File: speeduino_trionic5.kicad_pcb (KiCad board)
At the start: 2 copper layers, 152.4 x 127 mm, 30 parts, among them J3 trionic5_header, Q1 Q_NMOS_GDS, U1 Olimex_STM32-407_Extension_He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, U2 MCP2515_Breakout, U3 LM1815, U8 LM2940S-5.0/NOPB

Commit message: Boards should be placed correctly now
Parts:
- removed F1: Polyfuse, Fuse:Fuse_1812_4532Metric
- added D1: LED, LED_SMD:LED_0603_1608Metric, F.Cu at (-47.4, 109.2)
- added D10: LED, LED_SMD:LED_0603_1608Metric, F.Cu at (-35.2, 98.3)
- added D11: LED, LED_SMD:LED_0603_1608Metric, F.Cu at (-71.7, 125.3)
- added D12: LED, LED_SMD:LED_0603_1608Metric, F.Cu at (-79.8, 125.3)
- added D13: LED, LED_SMD:LED_0603_1608Metric, F.Cu at (-83.8, 125.3)
- added D16: LED, LED_SMD:LED_0603_1608Metric, F.Cu at (-35.2, 95.7)
- added D17: LED, LED_SMD:LED_0603_1608Metric, F.Cu at (-24.5, 114.3)
- added D18: LED, LED_SMD:LED_0603_1608Metric, F.Cu at (-20.4, 114.3)
- added D3: LED, LED_SMD:LED_0603_1608Metric, F.Cu at (-59.5, 119.9)
- added D4: LED, LED_SMD:LED_0603_1608Metric, F.Cu at (-55.5, 117.3)
- added D5: LED, LED_SMD:LED_0603_1608Metric, F.Cu at (-75.7, 125.3)
- added D6: LED, LED_SMD:LED_0603_1608Metric, F.Cu at (-63.6, 125.3)
- added D7: LED, LED_SMD:LED_0603_1608Metric, F.Cu at (-59.5, 117.3)
- added D8: LED, LED_SMD:LED_0603_1608Metric, F.Cu at (-67.6, 125.3)
- added D9: LED, LED_SMD:LED_0603_1608Metric, F.Cu at (-35.2, 93.1)
- added Q1: Q_NMOS_GDS, Package_TO_SOT_SMD:TO-252-2, F.Cu at (-55.5, 103.9)
- added Q10: Q_NMOS_GDS, Package_TO_SOT_SMD:TO-252-2, F.Cu at (-67.7, 112.0)
- added Q11: Q_NMOS_GDS, Package_TO_SOT_SMD:TO-252-2, F.Cu at (-79.8, 103.9)
- added Q12: Q_NMOS_GDS, Package_TO_SOT_SMD:TO-252-2, F.Cu at (-43.4, 103.9)
- added Q13: Q_NMOS_GDS, Package_TO_SOT_SMD:TO-252-2, F.Cu at (-67.7, 103.9)
- added Q14: Q_NMOS_GDS, Package_TO_SOT_SMD:TO-252-2, F.Cu at (-20.4, 109.0)
- added Q15: Q_NMOS_GDS, Package_TO_SOT_SMD:TO-252-2, F.Cu at (-8.04, 103.1)
- added Q2: Q_NMOS_GDS, Package_TO_SOT_SMD:TO-252-2, F.Cu at (-79.8, 120.0)
- added Q3: Q_NMOS_GDS, Package_TO_SOT_SMD:TO-252-2, F.Cu at (-67.7, 120.0)
- added Q4: Q_NMOS_GDS, Package_TO_SOT_SMD:TO-252-2, F.Cu at (-79.8, 95.8)
- added Q5: Q_NMOS_GDS, Package_TO_SOT_SMD:TO-252-2, F.Cu at (-55.5, 112.0)
- added Q6: Q_NMOS_GDS, Package_TO_SOT_SMD:TO-252-2, F.Cu at (-43.4, 95.8)
- added Q7: Q_NMOS_GDS, Package_TO_SOT_SMD:TO-252-2, F.Cu at (-67.7, 95.8)
- added Q8: Q_NMOS_GDS, Package_TO_SOT_SMD:TO-252-2, F.Cu at (-55.5, 95.8)
- added Q9: Q_NMOS_GDS, Package_TO_SOT_SMD:TO-252-2, F.Cu at (-79.8, 112.0)
- added R10: 1k, Resistor_SMD:R_0603_1608Metric, F.Cu at (-27.2, 98.1)
- added R11: 1k, Resistor_SMD:R_0603_1608Metric, F.Cu at (-31.2, 93.1)
- added R12: 1k, Resistor_SMD:R_0603_1608Metric, F.Cu at (-47.4, 116.8)
- added R13: 1k, Resistor_SMD:R_0603_1608Metric, F.Cu at (-31.2, 95.6)
- added R14: 1k, Resistor_SMD:R_0603_1608Metric, F.Cu at (-27.2, 93.1)
- added R15: 1k, Resistor_SMD:R_0603_1608Metric, F.Cu at (-47.4, 114.3)
- added R16: 1k, Resistor_SMD:R_0603_1608Metric, F.Cu at (-43.4, 109.2)
- added R17: 1k, Resistor_SMD:R_0603_1608Metric, F.Cu at (-35.3, 103.4)
- added R18: 1k, Resistor_SMD:R_0603_1608Metric, F.Cu at (-35.3, 100.8)
- added R19: 1k, Resistor_SMD:R_0603_1608Metric, F.Cu at (-55.5, 122.3)
- added R20: 1k, Resistor_SMD:R_0603_1608Metric, F.Cu at (-39.4, 109.2)
- added R21: 1k, Resistor_SMD:R_0603_1608Metric, F.Cu at (-59.6, 122.4)
- added R22: 1k, Resistor_SMD:R_0603_1608Metric, F.Cu at (-23.2, 93.1)
- added R23: 1k, Resistor_SMD:R_0603_1608Metric, F.Cu at (-51.5, 122.2)
- added R24: 1k, Resistor_SMD:R_0603_1608Metric, F.Cu at (-27.2, 95.6)
- added R25: 1k, Resistor_SMD:R_0603_1608Metric, F.Cu at (-59.6, 124.9)
- added R26: 1k, Resistor_SMD:R_0603_1608Metric, F.Cu at (-55.6, 124.8)
- added R27: 1k, Resistor_SMD:R_0603_1608Metric, F.Cu at (-51.5, 119.7)
- added R28: 1k, Resistor_SMD:R_0603_1608Metric, F.Cu at (-43.4, 114.3)
- added R29: 1k, Resistor_SMD:R_0603_1608Metric, F.Cu at (-47.4, 111.8)
- added R30: 1k, Resistor_SMD:R_0603_1608Metric, F.Cu at (-31.2, 98.1)
- added R31: 1k, Resistor_SMD:R_0603_1608Metric, F.Cu at (-55.5, 119.8)
- added R32: 1k, Resistor_SMD:R_0603_1608Metric, F.Cu at (-35.3, 105.9)
- added R33: 1k, Resistor_SMD:R_0603_1608Metric, F.Cu at (-16.5, 116.8)
- added R34: 1k, Resistor_SMD:R_0603_1608Metric, F.Cu at (-12.5, 114.3)
- added R35: 1k, Resistor_SMD:R_0603_1608Metric, F.Cu at (-20.5, 116.8)
- added R36: 1k, Resistor_SMD:R_0603_1608Metric, F.Cu at (-24.5, 116.8)
- added R7: 1k, Resistor_SMD:R_0603_1608Metric, F.Cu at (-31.3, 100.8)
- added R8: 1k, Resistor_SMD:R_0603_1608Metric, F.Cu at (-51.5, 117.2)
- added R9: 1k, Resistor_SMD:R_0603_1608Metric, F.Cu at (-43.4, 111.8)
- J3: moved to B.Cu
- U1, XA1, XA2: moved to F.Cu
- U8: footprint Package_TO_SOT_SMD:TO-263-3_TabPin2 -> Package_TO_SOT_SMD:SOT-223
- moved J3 90.7 mm to (71.8, 35.0), turned to 0 degrees
- moved U1 85.7 mm to (106.7, 68.6), turned to 0 degrees
- moved XA2 56.4 mm to (175.3, 132.1)
- moved XA1 49.9 mm to (96.5, 149.9)
- moved D2 48.7 mm to (-55.0, 149.9)
- moved U8 26.7 mm to (-45.7, 25.4)
- moved C17 16.2 mm to (-41.1, 44.7)
- moved D15 16.2 mm to (-24.2, 32.2)
- moved C21 16.2 mm to (-17.0, 31.6)
- moved C18 16.2 mm to (-25.9, 41.4)
- moved C20 16.2 mm to (-19.2, 36.4)
- moved D14 16.2 mm to (-32.2, 44.0)
- moved Q1 15.5 mm to (-29.6, 152.4)
- moved R3 15.5 mm to (-33.2, 143.0)
- moved R4 15.5 mm to (-32.0, 126.4)
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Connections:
- net VDD renamed Net-(C20-Pad1)
- J3 pad 10: unconnected-(J3-Pad10) -> T5_IGN2
- J3 pad 11: unconnected-(J3-Pad11) -> T5_IGN3
- J3 pad 12: unconnected-(J3-Pad12) -> T5_IGN4
- J3 pad 17: unconnected-(J3-Pad17) -> T5_COMB12
- J3 pad 18: unconnected-(J3-Pad18) -> T5_COMB34
- J3 pad 2: unconnected-(J3-Pad2) -> T5_APCA
- J3 pad 22: unconnected-(J3-Pad22) -> T5_MAP
- J3 pad 23: unconnected-(J3-Pad23) -> T5_O2_1
- J3 pad 26: unconnected-(J3-Pad26) -> T5_APCB
- J3 pad 3: unconnected-(J3-Pad3) -> T5_INJ1
- J3 pad 31: unconnected-(J3-Pad31) -> T5_MAINRLY
- J3 pad 32: unconnected-(J3-Pad32) -> T5_CHECKENG
- J3 pad 4: unconnected-(J3-Pad4) -> T5_INJ2
- J3 pad 41: unconnected-(J3-Pad41) -> T5_CPS
- J3 pad 42: unconnected-(J3-Pad42) -> +5V
- J3 pad 43: unconnected-(J3-Pad43) -> +5V
- J3 pad 44: unconnected-(J3-Pad44) -> T5_KNOCK
- J3 pad 45: unconnected-(J3-Pad45) -> T5_TPS
- J3 pad 46: unconnected-(J3-Pad46) -> T5_IAT
- J3 pad 49: unconnected-(J3-Pad49) -> T5_IAC
- J3 pad 5: unconnected-(J3-Pad5) -> T5_INJ3
- J3 pad 55: unconnected-(J3-Pad55) -> T5_SHIFTUP
- J3 pad 56: unconnected-(J3-Pad56) -> T5_FUELRLY
- J3 pad 6: unconnected-(J3-Pad6) -> T5_INJ4
- J3 pad 66: unconnected-(J3-Pad66) -> GND
- J3 pad 67: unconnected-(J3-Pad67) -> GND
- J3 pad 68: unconnected-(J3-Pad68) -> T5_COOLANT
- J3 pad 70: unconnected-(J3-Pad70) -> T5_O2_2
- J3 pad 9: unconnected-(J3-Pad9) -> T5_IGN1
- U2 pad 6: unconnected-(U2-Pad6) -> GND
- U2 pad 7: unconnected-(U2-Pad7) -> +3.3V
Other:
- outline, holes or cut-outs redrawn

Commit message: Low side drivers mostly in order
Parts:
- removed the D1 at (-38.0, 137.9)
- removed the D1 at (-21.5, 149.7)
- removed the D1 at (-47.4, 109.2)
- removed the Q1 at (-55.5, 103.9)
- removed the Q1 at (-29.6, 152.4)
- removed the R7 at (-31.3, 100.8)
- removed the R7 at (-21.5, 152.2)
- removed the R7 at (-32.7, 136.9)
- removed the R8 at (-51.5, 117.2)
- removed the R8 at (-21.5, 154.7)
- added D1: LED, LED_SMD:LED_0603_1608Metric, F.Cu at (108.5, 60.8)
- added Q1: Q_NMOS_GDS, Package_TO_SOT_SMD:TO-252-2, F.Cu at (103.9, 56.7)
- added R7: 1k, Resistor_SMD:R_0603_1608Metric, F.Cu at (108.5, 53.7)
- added R8: 1k, Resistor_SMD:R_0603_1608Metric, F.Cu at (101.4, 47.1)
- U2: moved to F.Cu
- moved D13 281.1 mm to (182.1, 34.0)
- moved Q9 263.9 mm to (178.2, 56.9)
- moved Q13 252.2 mm to (178.2, 47.8)
- moved R21 244.0 mm to (174.2, 52.3), turned to 180 degrees
- moved R31 242.2 mm to (174.2, 43.2), turned to 180 degrees
- moved R27 241.4 mm to (174.2, 34.1), turned to 180 degrees
- moved Q12 231.0 mm to (178.2, 38.6)
- moved D12 225.4 mm to (128.8, 40.0), turned to 90 degrees
- moved D16 223.6 mm to (182.1, 43.2)
- moved R32 223.0 mm to (178.7, 43.2)
- moved D10 222.2 mm to (182.2, 52.3)
- moved Q11 221.6 mm to (133.4, 43.6), turned to 90 degrees
- moved R30 219.5 mm to (178.7, 34.0)
- moved D11 217.4 mm to (135.9, 60.8), turned to -90 degrees
- moved D2 212.2 mm to (146.6, 83.7)
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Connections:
- Q3 pad 1: MCU_IGN1 -> MCU_APCA
- R9 pad 1: MCU_IGN1 -> MCU_APCA
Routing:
- net T5_IAC: track 0.00 -> 128.5 mm, vias 0 -> 1
- net GND: track 0.00 -> 126.7 mm
- net +3.3V: track 0.00 -> 117.2 mm, vias 0 -> 5
- net T5_MAINRLY: track 0.00 -> 83.8 mm, vias 0 -> 2
- net T5_FUELRLY: track 0.00 -> 69.0 mm, vias 0 -> 2
- net T5_INJ4: track 0.00 -> 62.3 mm, vias 0 -> 2
- net T5_INJ3: track 0.00 -> 54.9 mm, vias 0 -> 2
- net T5_INJ2: track 0.00 -> 47.8 mm, vias 0 -> 2
- net T5_INJ1: track 0.00 -> 44.9 mm, vias 0 -> 2
- net T5_APCA: track 0.00 -> 39.0 mm
- net T5_APCB: track 0.00 -> 38.0 mm
- net T5_IGN4: track 0.00 -> 29.8 mm
- net MCU_IGN2: track 0.00 -> 20.7 mm, vias 0 -> 1
- net T5_IGN3: track 0.00 -> 19.8 mm
- net MCU_IGN4: track 0.00 -> 19.7 mm, vias 0 -> 1
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
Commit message: Add JLCPCB Components
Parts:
- added R37: 10k, Resistor_SMD:R_0603_1608Metric, F.Cu at (70.3, 123.0)
- added R38: 20k, Resistor_SMD:R_0603_1608Metric, F.Cu at (62.3, 125.5)
- added R39: 20k, Resistor_SMD:R_0603_1608Metric, F.Cu at (66.3, 125.5)
- added R40: 1k, Resistor_SMD:R_0603_1608Metric, F.Cu at (70.3, 128.1)
- added R41: 10k, Resistor_SMD:R_0603_1608Metric, F.Cu at (74.3, 120.5)
- added R42: 10k, Resistor_SMD:R_0603_1608Metric, F.Cu at (62.3, 120.5)
- added R43: 10k, Resistor_SMD:R_0603_1608Metric, F.Cu at (62.3, 123.0)
- added R44: 10k, Resistor_SMD:R_0603_1608Metric, F.Cu at (70.3, 120.5)
- added R45: 20k, Resistor_SMD:R_0603_1608Metric, F.Cu at (66.3, 123.0)
- added R46: 40k, Resistor_SMD:R_0603_1608Metric, F.Cu at (74.3, 125.5)
- added R47: 1k, Resistor_SMD:R_0603_1608Metric, F.Cu at (62.3, 128.1)
- added R48: 10k, Resistor_SMD:R_0603_1608Metric, F.Cu at (70.3, 125.5)
- added R49: 10k, Resistor_SMD:R_0603_1608Metric, F.Cu at (66.3, 120.5)
- added R50: 20k, Resistor_SMD:R_0603_1608Metric, F.Cu at (74.3, 123.0)
- added R51: 40k, Resistor_SMD:R_0603_1608Metric, F.Cu at (66.3, 128.1)
- C2: value 10nF -> 18nF
- R4: value 100k -> 180k
- moved C1 13.1 mm to (159.6, 89.8)
- moved R6 9.94 mm to (155.1, 91.3)
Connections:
- J3 pad 68: T5_COOLANT -> MCU_COOLANT
- R6 pad 1: +3.3V -> Net-(C3-Pad1)
- R6 pad 2: Net-(C3-Pad1) -> +3.3V

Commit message: More changes
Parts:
- added R52: 10k, Resistor_SMD:R_0603_1608Metric, F.Cu at (136.4, 69.2)
- added R53: 10k, Resistor_SMD:R_0603_1608Metric, F.Cu at (68.5, 74.7)
- added R54: 40k, Resistor_SMD:R_0603_1608Metric, F.Cu at (136.4, 70.8)
- added R55: 40k, Resistor_SMD:R_0603_1608Metric, F.Cu at (68.5, 76.3)
- moved R38 108.4 mm to (153.9, 67.7), turned to -90 degrees
- moved R47 103.4 mm to (149.9, 73.1)
- moved R37 101.7 mm to (155.6, 67.7), turned to 90 degrees
- moved R40 99.6 mm to (150.0, 68.2)
- moved R45 98.2 mm to (149.9, 71.5)
- moved R43 97.0 mm to (149.9, 81.4)
- moved R39 95.3 mm to (149.9, 79.8)
- moved R48 93.5 mm to (149.9, 76.5), turned to 180 degrees
- moved D14 91.6 mm to (69.1, 70.1), turned to 90 degrees
- moved R41 91.0 mm to (149.9, 69.8), turned to 180 degrees
- moved R44 90.2 mm to (149.9, 78.2), turned to 180 degrees
- moved R50 89.7 mm to (149.9, 74.8)
- moved R42 87.4 mm to (136.4, 74.1)
- moved C21 86.7 mm to (75.1, 81.2), turned to 180 degrees
- moved R51 86.5 mm to (136.4, 77.3), turned to 180 degrees
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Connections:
- net VRegIn renamed Net-(C17-Pad1)
- C20 pad 1: Net-(C20-Pad1) -> +5V
- C21 pad 1: Net-(C20-Pad1) -> +5V
- D14 pad 2: 12V-SW -> +30
- J3 pad 1: unconnected-(J3-Pad1) -> +30
- J3 pad 19: unconnected-(J3-Pad19) -> T5_WBO2
- J3 pad 24: unconnected-(J3-Pad24) -> GND
- J3 pad 25: unconnected-(J3-Pad25) -> GND
- J3 pad 46: T5_IAT -> MCU_IAT
- J3 pad 48: unconnected-(J3-Pad48) -> +30
- J3 pad 60: unconnected-(J3-Pad60) -> +15
- R40 pad 1: T5_IAT -> MCU_IAT
- U2 pad 1: unconnected-(U2-Pad1) -> CAN_INT
- U2 pad 2: unconnected-(U2-Pad2) -> SCK
- U2 pad 3: unconnected-(U2-Pad3) -> MOSI
- U2 pad 4: unconnected-(U2-Pad4) -> MISO
- U2 pad 5: unconnected-(U2-Pad5) -> CAN_CS
- U8 pad 3: Net-(C20-Pad1) -> +5V
- XA1 pad 3V3: unconnected-(XA1-Pad3V3) -> +3.3V
- XA1 pad 5V1: unconnected-(XA1-Pad5V1) -> +5V
- XA1 pad 5V3: unconnected-(XA1-Pad5V3) -> +5V
- XA1 pad 5V4: unconnected-(XA1-Pad5V4) -> +5V
- XA1 pad A0: unconnected-(XA1-PadA0) -> MCU_IAT
- XA1 pad A1: unconnected-(XA1-PadA1) -> MCU_COOLANT
- XA1 pad A2: unconnected-(XA1-PadA2) -> MCU_TPS
- XA1 pad A3: unconnected-(XA1-PadA3) -> MCU_MAP
- XA1 pad A4: unconnected-(XA1-PadA4) -> MCU_BAT
- XA1 pad A8: unconnected-(XA1-PadA8) -> MCU_WBO2
- XA1 pad D18: unconnected-(XA1-PadD18) -> MCU_COMB12
- XA1 pad D19: unconnected-(XA1-PadD19) -> MCU_COMB34
- XA1 pad D2: unconnected-(XA1-PadD2) -> MCU_IGN_+15
- XA1 pad D20: unconnected-(XA1-PadD20) -> CAN_INT
- XA1 pad D22: unconnected-(XA1-PadD22) -> MCU_FUELRLY
- XA1 pad D23: unconnected-(XA1-PadD23) -> MCU_MAINRLY
- XA1 pad D44: unconnected-(XA1-PadD44) -> MCU_APCA
- XA1 pad D45: unconnected-(XA1-PadD45) -> MCU_APCB
- XA1 pad D50: unconnected-(XA1-PadD50) -> MISO
- XA1 pad D51: unconnected-(XA1-PadD51) -> MOSI
- XA1 pad D52: unconnected-(XA1-PadD52) -> SCK
- XA1 pad D53: unconnected-(XA1-PadD53) -> CAN_CS
- XA1 pad GND1: unconnected-(XA1-PadGND1) -> GND
- XA1 pad GND2: unconnected-(XA1-PadGND2) -> GND
- XA1 pad GND3: unconnected-(XA1-PadGND3) -> GND
- XA1 pad GND5: unconnected-(XA1-PadGND5) -> GND
- XA1 pad GND6: unconnected-(XA1-PadGND6) -> GND
- XA2 pad 3V3: unconnected-(XA2-Pad3V3) -> +3.3V
- XA2 pad 5V1: unconnected-(XA2-Pad5V1) -> +5V
- XA2 pad GND1: unconnected-(XA2-PadGND1) -> GND
- XA2 pad GND2: unconnected-(XA2-PadGND2) -> GND
- XA2 pad GND3: unconnected-(XA2-PadGND3) -> GND
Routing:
- net GND: track 126.7 -> 531.3 mm, vias 0 -> 6
- net +5V: track 0.00 -> 362.1 mm, vias 0 -> 1
- net +3.3V: track 117.2 -> 477.4 mm, vias 5 -> 11
- net MCU_INJ4: track 14.1 -> 148.3 mm, vias 1 -> 3
- net MCU_FUELRLY: track 2.69 -> 131.3 mm, vias 0 -> 3
- net MCU_INJ3: track 14.1 -> 134.7 mm, vias 1 -> 3
- net MCU_MAINRLY: track 2.69 -> 122.9 mm, vias 0 -> 3
- net MCU_IGN4: track 19.7 -> 139.3 mm, vias 1 -> 2
- net MCU_INJ2: track 14.9 -> 124.6 mm, vias 1 -> 3
- net MCU_IGN3: track 19.6 -> 126.8 mm, vias 1 -> 2
- net +30: track 0.00 -> 105.7 mm, vias 0 -> 1
- net MCU_INJ1: track 13.9 -> 113.4 mm, vias 1 -> 3
- net MCU_IGN2: track 20.7 -> 116.2 mm, vias 1 -> 2
- net T5_SHIFTUP: track 5.57 -> 96.8 mm, vias 0 -> 1
- net MCU_IGN1: track 19.2 -> 107.3 mm, vias 1 -> 2
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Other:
- outline, holes or cut-outs redrawn
- board text added: "Arduino_Uno_R3_Shield"

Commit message: Add stuff
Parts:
- added U4: TCAN330, Package_TO_SOT_SMD:SOT-23-8, F.Cu at (187.7, 55.9)
- XA1: footprint PCM_arduino-library:Arduino_Mega2560_Shield -> arduino-library:Arduino_Mega2560_Shield
- XA2: footprint PCM_arduino-library:Arduino_Uno_R3_Shield -> arduino-library:Arduino_Uno_R3_Shield
- moved R37 2.00 mm to (155.4, 69.7)
- moved R38 2.00 mm to (153.8, 69.7)
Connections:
- XA2 pad A0: unconnected-(XA2-PadA0) -> MCU_IAT
- XA2 pad A1: unconnected-(XA2-PadA1) -> MCU_COOLANT
- XA2 pad A2: unconnected-(XA2-PadA2) -> MCU_TPS
- XA2 pad A3: unconnected-(XA2-PadA3) -> MCU_MAP
- XA2 pad A4: unconnected-(XA2-PadA4) -> MCU_BAT
- XA2 pad A5: unconnected-(XA2-PadA5) -> MCU_WBO2
- XA2 pad D0: unconnected-(XA2-PadD0) -> MCU_CANRX
- XA2 pad D1: unconnected-(XA2-PadD1) -> MCU_CANTX
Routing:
- net GND: track 531.3 -> 707.7 mm, vias 6 -> 10
- net +3.3V: track 477.4 -> 555.7 mm, vias 11 -> 16
- net MCU_BAT: track 1.63 -> 30.2 mm, vias 0 -> 1
- net +30: track 105.7 -> 98.2 mm
- net CANH: track 81.3 -> 88.3 mm
- net CANL: track 79.9 -> 84.1 mm
- net MCU_MAINRLY: track 122.9 -> 125.3 mm
- net MCU_FUELRLY: track 131.3 -> 133.0 mm
- net MCU_INJ4: track 148.3 -> 149.9 mm
- net T5_MAP: track 48.8 -> 50.1 mm
- net MCU_COOLANT: track 54.6 -> 55.4 mm
- net MCU_IGN1: track 107.3 -> 108.1 mm
- net T5_TPS: track 49.3 -> 49.8 mm

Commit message: Basically done!
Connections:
- R49 pad 1: MCU_COM34 -> MCU_COMB34
- R51 pad 2: MCU_COM34 -> MCU_COMB34
- U1 pad 15: unconnected-(U1-Pad15) -> MCU_INJ1
- U1 pad 16: unconnected-(U1-Pad16) -> MCU_INJ2
- U1 pad 17: unconnected-(U1-Pad17) -> MCU_INJ3
- U1 pad 18: unconnected-(U1-Pad18) -> MCU_INJ4
- U1 pad 32: unconnected-(U1-Pad32) -> MCU_IGN1
- U1 pad 34: unconnected-(U1-Pad34) -> MCU_IGN2
- U1 pad 36: unconnected-(U1-Pad36) -> MCU_IGN3
- U1 pad 37: unconnected-(U1-Pad37) -> MCU_IGN4
- XA1 pad AREF: unconnected-(XA1-PadAREF) -> +3.3V
- XA2 pad D11: unconnected-(XA2-PadD11) -> MCU_COMB12
- XA2 pad D12: unconnected-(XA2-PadD12) -> MCU_CPS
- XA2 pad D13: unconnected-(XA2-PadD13) -> MCU_COMB34
- XA2 pad D4: unconnected-(XA2-PadD4) -> MCU_APCA
- XA2 pad D5: unconnected-(XA2-PadD5) -> MCU_APCB
- XA2 pad D6: unconnected-(XA2-PadD6) -> MCU_MAINRLY
- XA2 pad D7: unconnected-(XA2-PadD7) -> MCU_FUELRLY
- XA2 pad D8: unconnected-(XA2-PadD8) -> MCU_IGN_+15
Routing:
- net CAN_INT: track 0.00 -> 285.8 mm, vias 0 -> 4
- net MCU_WBO2: track 1.68 -> 203.7 mm, vias 0 -> 4
- net MCU_COMB34: track 0.00 -> 195.7 mm, vias 0 -> 4
- net MCU_COMB12: track 1.68 -> 196.4 mm, vias 0 -> 2
- net MCU_TPS: track 1.64 -> 182.0 mm, vias 0 -> 3
- net MCU_IAT: track 50.6 -> 230.3 mm, vias 1 -> 3
- net MCU_COOLANT: track 55.4 -> 234.5 mm, vias 1 -> 3
- net MCU_MAP: track 1.66 -> 179.9 mm, vias 0 -> 1
- net MCU_IGN_+15: track 1.65 -> 176.0 mm, vias 0 -> 2
- net MCU_BAT: track 30.2 -> 201.5 mm, vias 1 -> 3
- net MCU_CPS: track 17.0 -> 181.6 mm, vias 2 -> 4
- net CAN_CS: track 0.00 -> 111.9 mm, vias 0 -> 4
- net MOSI: track 0.00 -> 107.0 mm, vias 0 -> 4
- net MISO: track 0.00 -> 104.0 mm, vias 0 -> 4
- net SCK: track 0.00 -> 102.1 mm, vias 0 -> 4
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
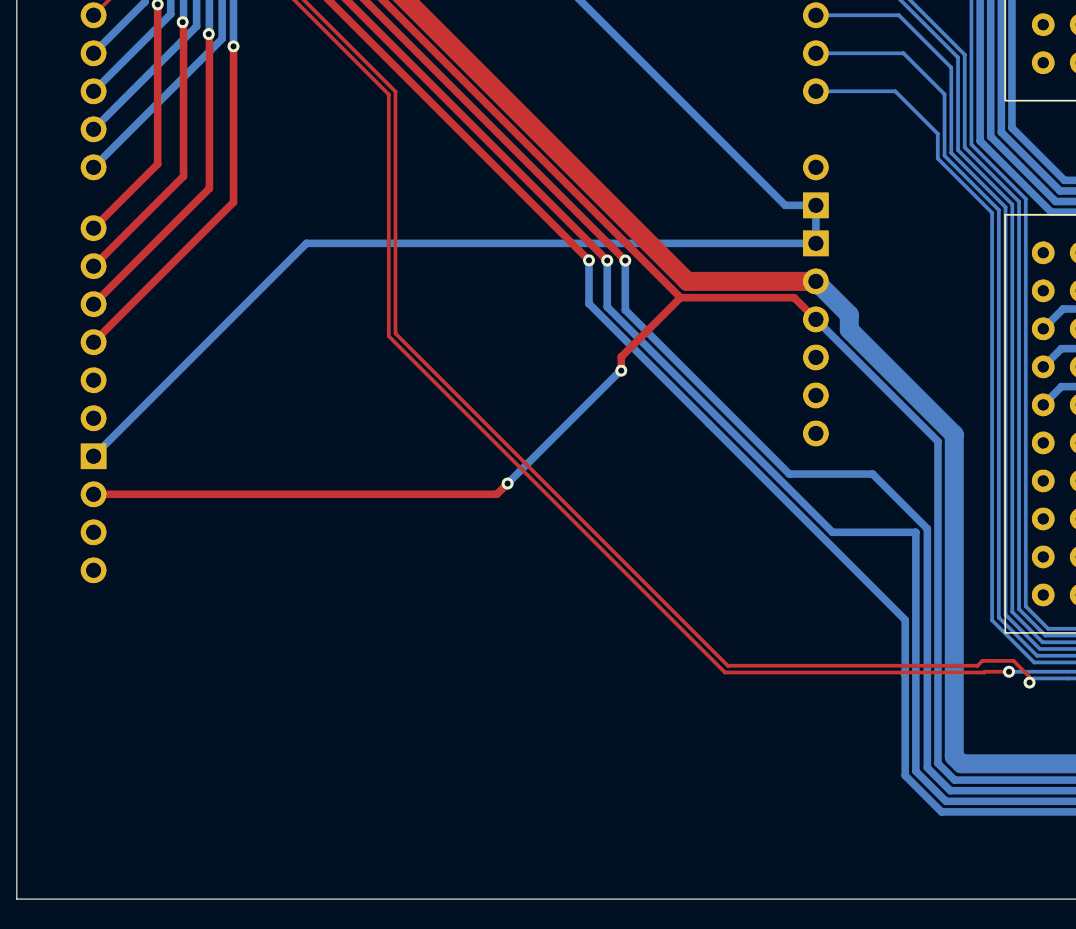
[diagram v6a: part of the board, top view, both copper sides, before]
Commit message: Added solderable breadboard area
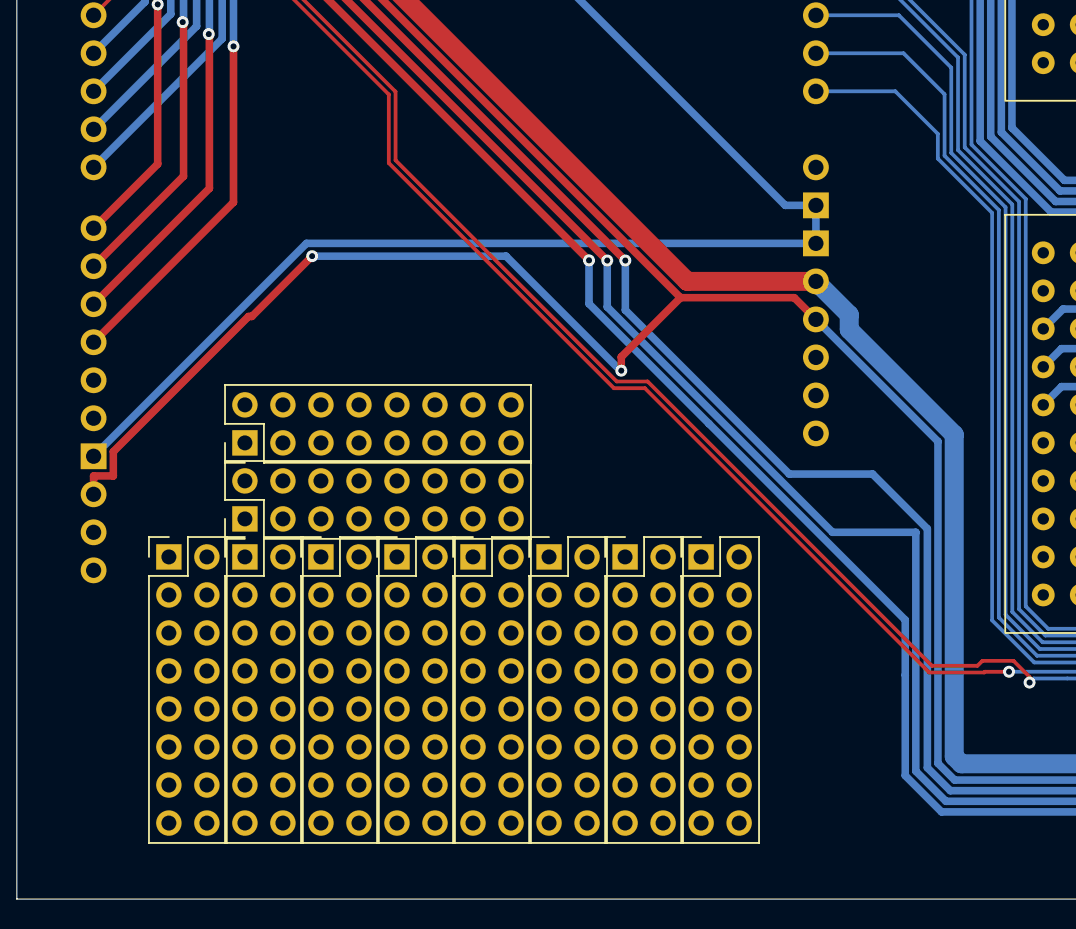
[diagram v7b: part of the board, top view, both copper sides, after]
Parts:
- added REF**: PinHeader_2x08_P2.54mm_Vertical, Connector_PinHeader_2.54mm:PinHeader_2x08_P2.54mm_Vertical, F.Cu at (50.8, 127.0)
- added REF**: PinHeader_2x08_P2.54mm_Vertical, Connector_PinHeader_2.54mm:PinHeader_2x08_P2.54mm_Vertical, F.Cu at (66.0, 127.0)
- added REF**: PinHeader_2x08_P2.54mm_Vertical, Connector_PinHeader_2.54mm:PinHeader_2x08_P2.54mm_Vertical, F.Cu at (55.9, 119.4)
- added REF**: PinHeader_2x08_P2.54mm_Vertical, Connector_PinHeader_2.54mm:PinHeader_2x08_P2.54mm_Vertical, F.Cu at (55.9, 127.0)
- added REF**: PinHeader_2x08_P2.54mm_Vertical, Connector_PinHeader_2.54mm:PinHeader_2x08_P2.54mm_Vertical, F.Cu at (76.2, 127.0)
- added REF**: PinHeader_2x08_P2.54mm_Vertical, Connector_PinHeader_2.54mm:PinHeader_2x08_P2.54mm_Vertical, F.Cu at (81.3, 127.0)
- added REF**: PinHeader_2x08_P2.54mm_Vertical, Connector_PinHeader_2.54mm:PinHeader_2x08_P2.54mm_Vertical, F.Cu at (61.0, 127.0)
- added REF**: PinHeader_2x08_P2.54mm_Vertical, Connector_PinHeader_2.54mm:PinHeader_2x08_P2.54mm_Vertical, F.Cu at (55.9, 124.5)
- added REF**: PinHeader_2x08_P2.54mm_Vertical, Connector_PinHeader_2.54mm:PinHeader_2x08_P2.54mm_Vertical, F.Cu at (86.4, 127.0)
- added REF**: PinHeader_2x08_P2.54mm_Vertical, Connector_PinHeader_2.54mm:PinHeader_2x08_P2.54mm_Vertical, F.Cu at (71.1, 127.0)
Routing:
- net +3.3V: track 601.0 -> 609.0 mm
- net MCU_IGN_+15: track 176.0 -> 169.2 mm
- net MCU_CPS: track 181.6 -> 174.8 mm
